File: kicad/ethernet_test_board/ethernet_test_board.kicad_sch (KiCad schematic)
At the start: 13 parts, among them J1 USB_C_Receptacle_USB2.0_16P, U1 W55RP20, U2 RT9080

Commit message: [add] kicad sch (finish) kicad pcb (WIP)
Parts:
- added C10, C11: 6.8n, Capacitor_SMD:C_0603_1608Metric, symbol Device:C
- added C12: 10n, Capacitor_SMD:C_0603_1608Metric, symbol Device:C
- added C13, C14: 18p, Capacitor_SMD:C_0603_1608Metric, symbol Device:C
- added C15, C16: 1μ, Capacitor_SMD:C_0603_1608Metric, symbol Device:C
- added C17, C18, C19, C20, C21: C, Capacitor_SMD:C_0603_1608Metric_Pad1.08x0.95mm_HandSolder, symbol Device:C
- added C5: 0.1μ, Capacitor_SMD:C_0603_1608Metric, symbol Device:C
- added C6: 0.1u, Capacitor_SMD:C_0603_1608Metric, symbol Device:C
- added C7: 10μ, Capacitor_SMD:C_0603_1608Metric, symbol Device:C
- added C8: 15p, Capacitor_SMD:C_0603_1608Metric, symbol Device:C
- added C9: 22n, Capacitor_SMD:C_0603_1608Metric, symbol Device:C
- added D1, D2: LED, Capacitor_SMD:C_0603_1608Metric, symbol Device:LED
- added D3: D, Capacitor_SMD:C_0603_1608Metric_Pad1.08x0.95mm_HandSolder, symbol Device:D
- added D4: LED, LED_SMD:LED_0603_1608Metric, symbol Device:LED
- added J2: Conn_01x02_Pin, ILG:ILG2pin, symbol Connector:Conn_01x02_Pin
- added J3, J5: TMJD4152NENLC, TMJD4152NENLC:TMJD4152NENLC, symbol TMJD4152NENLC:TMJD4152NENLC
- added J4: Conn_02x13_Top_Bottom, Connector_PinHeader_2.54mm:PinHeader_2x13_P2.54mm_Vertical, symbol Connector_Generic:Conn_02x13_Top_Bottom
- added J7: Micro_SD_Card_Det_Hirose_DM3AT, Connector_Card:microSD_HC_Hirose_DM3AT-SF-PEJM5, symbol Connector:Micro_SD_Card_Det_Hirose_DM3AT
- added J8: Conn_01x02_Pin, Connector_JST:JST_VH_B2P-VH-B_1x02_P3.96mm_Vertical, symbol Connector:Conn_01x02_Pin
- added R10, R11, R12, R13, R14, R9: 10K, Resistor_SMD:R_0603_1608Metric, symbol Device:R
- added R15: 100, Resistor_SMD:R_0603_1608Metric, symbol Device:R
- added R16, R17, R20, R21: 49.9, Capacitor_SMD:C_0603_1608Metric, symbol Device:R
- added R19: 10, Capacitor_SMD:C_0603_1608Metric, symbol Device:R
- added R22: 1M, Capacitor_SMD:C_0603_1608Metric, symbol Device:R
- added R23, R24: R, Capacitor_SMD:C_0603_1608Metric, symbol Device:R
- added R7: 10k, Resistor_SMD:R_0603_1608Metric, symbol Device:R
- added R8: 1k, Resistor_SMD:R_0603_1608Metric, symbol Device:R
- added SW1, SW2: SW_Push, Button_Switch_THT:SW_PUSH_6mm_H7.3mm, symbol Switch:SW_Push
- added U3: MCP25625-x-SS, Package_SO:SSOP-28_5.3x10.2mm_P0.65mm, symbol Interface_CAN_LIN:MCP25625-x-SS
- added U4: XC6201, Package_TO_SOT_SMD:SOT-23-5, symbol Regulator_Linear:XC6206PxxxMR
- added U5: SiT2001B, Package_TO_SOT_SMD:SOT-23-5, symbol Regulator_Linear:AP2127K-1.2
- added U6: LM66100DCKR, LM66100DCKR:SOT65P210X110-6N, symbol LM66100DCKR:LM66100DCKR
- added Y1: FA-128, Oscillator:Oscillator_SMD_SeikoEpson_SG210-4Pin_2.5x2.0mm, symbol Oscillator:SG-210SED
- C1, C2, C3, C4, R2, R3, R4, R5, R6: footprint (none) -> Capacitor_SMD:C_0603_1608Metric
- J1: footprint (none) -> Connector_USB:USB_C_Receptacle_GCT_USB4105-xx-A_16P_TopMnt_Horizontal
- R1: value 100k -> 1k; footprint (none) -> Capacitor_SMD:C_0603_1608Metric
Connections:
- net +3.3V: now also R2.1, C17.1, C18.1, C19.1, C20.1, C5.1, C6.1, C7.1, D4.2 (A), J3.11 (A_YELLOW), J3.13 (A_GREEN), J4.3 (Pin_3), J5.11 (A_YELLOW), J5.13 (A_GREEN), J7.4 (VDD), R10.2, R11.2, R12.2, R13.2, R14.2, R23.1, R24.2, R7.1, R9.2, U3.1 (VIO), U3.19 (VDD), U5.4 (NC); no longer U1.29 (RUN)
- net +5V: now also C16.1, C21.1, J4.4 (Pin_4), U3.27 (VDDA), U4.5 (VO), U6.6 (VOUT); no longer J1.A4 (VBUS), J1.A9 (VBUS), J1.B4 (VBUS), J1.B9 (VBUS)
- net GND: now also R3.2, C12.2, C13.2, C14.2, C15.2, C16.2, C17.2, C18.2, C19.2, C20.2, C21.2, C5.2, C6.2, C7.2, C8.2, C9.1, J3.10, J3.7, J4.26 (Pin_26), J5.10, J5.7, J7.11 (SHIELD), J7.6 (VSS), J7.9 (DET_B), J8.2 (Pin_2), R8.2, SW1.1, SW2.1, U3.10 (GND), U3.26 (VSS), U4.2 (GND), U5.1 (GND), U6.2 (GND), U6.3 (~{CE}), Y1.2 (GND), Y1.4 (GND)
- net USB_Minus: now also U1.57 (USB_DM); no longer R3.1
- net USB_Plus: now also U1.58 (UDB_DP); no longer R2.1
- net TXM: now reaches U1.1 (TXN)
- net TXM: now also J3.1 (TD-), J4.20 (Pin_20), J5.4 (RD-), R16.2
- net DAT3: now reaches U1.10 (GPIO5)
- net DAT3: now also J7.2 (DAT3/CD), R13.1
- net CLK: now reaches U1.11 (GPIO6)
- net CLK: now also J7.5 (CLK), R11.1
- net CMD: now reaches U1.12 (GPIO7)
- net CMD: now also J7.3 (CMD), R12.1
- net DAT1: now reaches U1.14 (GPIO8)
- net DAT1: now also J7.8 (DAT1), R9.1
- net DAT2: now reaches U1.15 (GPIO9)
- net DAT2: now also J7.1 (DAT2), R14.1
- net CAN_CLK: now reaches U1.16 (GPIO10)
- net CAN_CLK: now also U3.14 (SCK)
- net CAN_MOSI: now reaches U1.17 (GPIO11)
- net CAN_MOSI: now also U3.15 (SI)
- net CAN_MISO: now reaches U1.18 (GPIO12)
- net CAN_MISO: now also U3.16 (SO)
- net CAN_CS: now reaches U1.19 (GPIO13)
- net CAN_CS: now also U3.17 (~{CS})
- net TXP: now reaches U1.2 (TXP)
- net TXP: now also J3.3 (TD+), J4.21 (Pin_21), J5.6 (RD+), R17.2
- net CAN_STBY: now reaches U1.20 (GPIO14)
- net CAN_STBY: now also U3.5 (STBY)
- net GPIO15: now reaches U1.21 (GPIO15)
- net GPIO15: now also J4.18 (Pin_18)
- net CLK_OUT: now reaches U1.23 (XIN)
- net CLK_OUT: now also C8.1, U3.9 (OSC1), U5.5 (OUT)
- net SWCLK: now reaches U1.27 (SWCLK)
- net SWCLK: now also J4.24 (Pin_24)
- net SWD: now reaches U1.28 (SWD)
- net SWD: now also J4.25 (Pin_25)
- net GPIO16: now reaches U1.30 (GPIO16)
- net GPIO16: now also J4.19 (Pin_19)
- net SPEED: now reaches U1.36 (SPDLED)
- net SPEED: now also J3.12 (K_YELLOW), J5.12 (K_YELLOW)
- net LINK: now reaches U1.37 (LINKLED)
- net LINK: now also J3.14 (K_GREEN), J5.14 (K_GREEN)
- net DUPLEX: now reaches U1.38 (DUPLED)
- net DUPLEX: now also D2.1 (K)
- net ACTIVE: now reaches U1.39 (ACTLED)
- net ACTIVE: now also D1.1 (K)
- net RXM: now reaches U1.4 (RXN)
- net RXM: now also C10.1, J4.23 (Pin_23), R20.1
- net GPIO18: now reaches U1.40 (GPIO18)
- net GPIO18: now also J4.13 (Pin_13)
- net GPIO19: now reaches U1.41 (GPIO19)
- net GPIO19: now also J4.12 (Pin_12)
- net W5500_CLKIN: now reaches U1.44 (XI)
- net W5500_CLKIN: now also C14.1, R22.1, Y1.1 (OUT)
- net W5500_CLKOUT: now reaches U1.45 (XO)
- net W5500_CLKOUT: now also C13.1, R22.2, Y1.3 (OUT)
- net GPIO26: now reaches U1.46 (GPIO26/ADC0)
- net GPIO26: now also J4.11 (Pin_11)
- net GPIO27: now reaches U1.47 (GPIO27/ADC1)
- net GPIO27: now also J4.10 (Pin_10)
- net GPIO28: now reaches U1.48 (GPIO28/ADC2)
- net GPIO28: now also J4.9 (Pin_9)
- net GPIO29: now reaches U1.49 (GPIO29/ADC3)
- net GPIO29: now also J4.8 (Pin_8)
- net RXP: now reaches U1.5 (RXP)
- net RXP: now also C11.1, J4.22 (Pin_22), R21.1
- net PMODE2: now reaches U1.50 (PMODE2)
- net PMODE2: now also J4.5 (Pin_5)
- net PMODE1: now reaches U1.51 (PMODE1)
- net PMODE1: now also J4.6 (Pin_6)
- net PMODE0: now reaches U1.52 (PMODE0)
- net PMODE0: now also J4.7 (Pin_7)
- net at R2.2: now also U1.29 (RUN), SW1.2; no longer U1.58 (UDB_DP)
- net at R1.1, U1.63 (BOOT): now also SW2.2
- net GPIO0: now reaches U1.65 (GPIO0)
- net GPIO0: now also J4.14 (Pin_14)
- net GPIO1: now reaches U1.66 (GPIO1)
- net GPIO1: now also J4.15 (Pin_15)
- net GPIO2: now reaches U1.67 (GPIO2)
- net GPIO2: now also J4.16 (Pin_16)
- net GPIO3: now reaches U1.68 (GPIO3)
- net GPIO3: now also J4.17 (Pin_17)
- net DAT0: now reaches U1.9 (GPIO4)
- net DAT0: now also J7.7 (DAT0), R10.1
- new net: J7.10 (DET_A), R15.1
- new net: J2.1 (Pin_1), U3.3 (CANL)
- new net: J2.2 (Pin_2), U3.4 (CANH)
- new net: D1.2 (A), R23.2
- new net: D3.2 (A), J8.1 (Pin_1)
- new net: D4.1 (K), R15.2
- new net: C12.1, J3.5 (CT_2), J5.2 (CT_1), R20.2, R21.2
- new net: R7.2, U3.18 (~{RESET})
- new net: U3.20 (TxCAN), U3.28 (RXD)
- new net: U3.21 (RxCAN), U3.24 (TXD)
- new net: R8.1, U3.8 (OSC2)
- new net: C10.2, J3.4 (RD-), J5.1 (TD-)
- new net: C11.2, J3.6 (RD+), J5.3 (TD+)
- new net: C9.2, J3.2 (CT_1), J5.5 (CT_2), R19.2
- new net: R3.1, U6.5 (ST)
- new net: D2.2 (A), R24.1
- new net +3.3VA: R16.1, R17.1, R19.1
- new net +BATT: C15.1, D3.1 (K), J4.1 (Pin_1), U4.1 (VI)
- new net CAN_INT: U3.13 (~{INT})
- new net Ethernet_PoE: J3.9, J4.2 (Pin_2), J5.9
- new net USB_VCC: J1.A4 (VBUS), J1.A9 (VBUS), J1.B4 (VBUS), J1.B9 (VBUS), U6.1 (VIN)
- no-connect marks 3 -> 2
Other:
- note added: "GREEN_LINK"
- note added: "YELLOW_SPEED"
- note added: "microSD"
- moved on the sheet: C2, C3, R1, U2

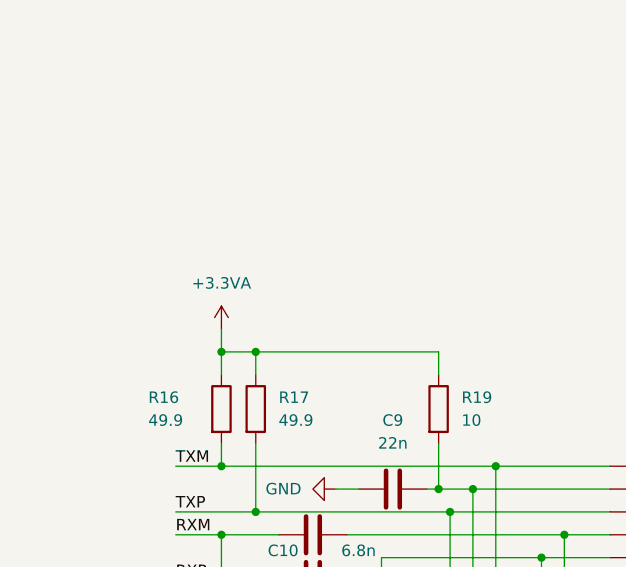
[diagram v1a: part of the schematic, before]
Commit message: [fix] kicad ethernet error
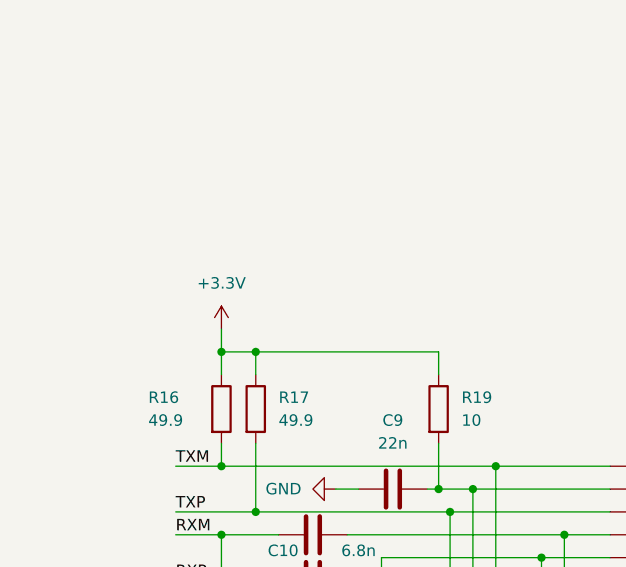
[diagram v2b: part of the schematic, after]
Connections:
- net +3.3VA is gone; now on net +3.3V: R16.1, R17.1, R19.1
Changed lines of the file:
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@@
 	)
 	(symbol
+		(lib_id "power:+3.3V")
+		(at -102.87 134.62 0)
+		(unit 1)
+		(exclude_from_sim no)
+		(in_bom yes)
+		(on_board yes)
+		(dnp no)
+		(fields_autoplaced yes)
+		(property "Reference" "#PWR034"
+			(at -102.87 138.43 0)
+			(effects
+				(font
+					(size 1.27 1.27)
+				)
+				(hide yes)
+			)
+		)
+		(property "Value" "+3.3V"
+			(at -102.87 129.54 0)
+			(effects
+				(font
+					(size 1.27 1.27)
+				)
+			)
+		)
+		(property "Footprint" ""
+			(at -102.87 134.62 0)
+			(effects
+				(font
+					(size 1.27 1.27)
+				)
+				(hide yes)
+			)
+		)
+		(property "Datasheet" ""
+			(at -102.87 134.62 0)
+			(effects
+				(font
+					(size 1.27 1.27)
+				)
+				(hide yes)
+			)
+		)
+		(property "Description" "Power symbol creates a global label with name \"+3.3V\""
+			(at -102.87 134.62 0)
+			(effects
+				(font
+					(size 1.27 1.27)
+				)
+				(hide yes)
+			)
+		)
+		(pin "1"
+		)
+		(instances
+			(project ""
+				(path "/72990fce-6b95-4e79-adfa-2df32c34bb5c"
+					(reference "#PWR034")
+					(unit 1)
+				)
+			)
+		)
+	)
+	(symbol
 		(lib_id "power:+5V")
 		(at 83.82 54.61 90)
@@
 					(unit 1)
 				)
-			)
-		)
-	)
-	(symbol
-		(lib_id "power:+3.3VA")
-		(at -102.87 134.62 0)
-		(unit 1)
-		(exclude_from_sim no)
-		(in_bom yes)
-		(on_board yes)
-		(dnp no)
-		(fields_autoplaced yes)
-		(property "Reference" "#PWR034"
-			(at -102.87 138.43 0)
-			(effects
-				(font
-					(size 1.27 1.27)
-				)
-				(hide yes)
-			)
-		)
-		(property "Value" "+3.3VA"
-			(at -102.87 129.54 0)
-			(effects
-				(font
-					(size 1.27 1.27)
-				)
-			)
-		)
-		(property "Footprint" ""
-			(at -102.87 134.62 0)
-			(effects
-				(font
-					(size 1.27 1.27)
-				)
-				(hide yes)
-			)
-		)
-		(property "Datasheet" ""
-			(at -102.87 134.62 0)
-			(effects
-				(font
-					(size 1.27 1.27)
-				)
-				(hide yes)
-			)
-		)
-		(property "Description" "Power symbol creates a global label with name \"+3.3VA\""
-			(at -102.87 134.62 0)
-			(effects
-				(font
-					(size 1.27 1.27)
-				)
-				(hide yes)
-			)
-		)
-		(pin "1"
-		)
-		(instances
-			(project ""
-				(path "/72990fce-6b95-4e79-adfa-2df32c34bb5c"
-					(reference "#PWR034")
-					(unit 1)
-				)

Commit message: [add] kicad pcb
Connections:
- net +5V: now also U6.3 (~{CE})
- net GND: no longer U6.3 (~{CE})
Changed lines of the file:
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@@
 	(wire
 		(pts
-			(xy 35.56 168.91) (xy 35.56 166.37)
-		)
-		(stroke
-			(width 0)
-			(type default)
-		)
-	)
-	(wire
-		(pts
 			(xy 323.85 69.85) (xy 314.96 69.85)
 		)
@@
 	)
 	(symbol
-		(lib_id "Connector_Generic:Conn_02x13_Top_Bottom")
-		(at 328.93 67.31 0)
-		(unit 1)
-		(exclude_from_sim no)
-		(in_bom yes)
-		(on_board yes)
-		(dnp no)
-		(fields_autoplaced yes)
-		(property "Reference" "J4"
-			(at 330.2 45.72 0)
-			(effects
-				(font
-					(size 1.27 1.27)
-				)
-			)
-		)
-		(property "Value" "Conn_02x13_Top_Bottom"
-			(at 330.2 48.26 0)
-			(effects
-				(font
-					(size 1.27 1.27)
-				)
-			)
-		)
-		(property "Footprint" "Connector_PinHeader_2.54mm:PinHeader_2x13_P2.54mm_Vertical"
-			(at 328.93 67.31 0)
-			(effects
-				(font
-					(size 1.27 1.27)
-				)
-				(hide yes)
-			)
-		)
-		(property "Datasheet" "~"
-			(at 328.93 67.31 0)
-			(effects
-				(font
-					(size 1.27 1.27)
-				)
-				(hide yes)
-			)
-		)
-		(property "Description" "Generic connector, double row, 02x13, top/bottom pin numbering scheme (row 1: 1...pins_per_row, row2: pins_per_row+1 ... num_pins), script generated (kicad-library-utils/schlib/autogen/connector/)"
-			(at 328.93 67.31 0)
-			(effects
-				(font
-					(size 1.27 1.27)
-				)
-				(hide yes)
-			)
-		)
-		(pin "26"
-		)
-		(pin "17"
-		)
-		(pin "19"
-		)
-		(pin "11"
-		)
-		(pin "12"
-		)
-		(pin "13"
-		)
-		(pin "4"
-		)
-		(pin "15"
-		)
-		(pin "14"
-		)
-		(pin "21"
-		)
-		(pin "2"
-		)
-		(pin "10"
-		)
-		(pin "1"
-		)
-		(pin "6"
-		)
-		(pin "5"
-		)
-		(pin "9"
-		)
-		(pin "16"
-		)
-		(pin "20"
-		)
-		(pin "25"
-		)
-		(pin "3"
-		)
-		(pin "22"
-		)
-		(pin "23"
-		)
-		(pin "8"
-		)
-		(pin "7"
-		)
-		(pin "18"
-		)
-		(pin "24"
-		)
-		(instances
-			(project ""
-				(path "/72990fce-6b95-4e79-adfa-2df32c34bb5c"
-					(reference "J4")
-					(unit 1)
-				)
-			)
-		)
-	)
-	(symbol
 		(lib_id "power:+3.3V")
 		(at 256.54 24.13 0)
@@
 	)
 	(symbol
+		(lib_id "Connector_Generic:Conn_02x13_Top_Bottom")
+		(at 328.93 67.31 0)
+		(unit 1)
+		(exclude_from_sim no)
+		(in_bom yes)
+		(on_board yes)
+		(dnp no)
+		(fields_autoplaced yes)
+		(property "Reference" "J4"
+			(at 330.2 45.72 0)
+			(effects
+				(font
+					(size 1.27 1.27)
+				)
+			)
+		)
+		(property "Value" "Conn_02x13_Top_Bottom"
+			(at 330.2 48.26 0)
+			(effects
+				(font
+					(size 1.27 1.27)
+				)
+			)
+		)
+		(property "Footprint" "Connector_PinHeader_2.54mm:PinHeader_2x13_P2.54mm_Vertical"
+			(at 328.93 67.31 0)
+			(effects
+				(font
+					(size 1.27 1.27)
+				)
+				(hide yes)
+			)
+		)
+		(property "Datasheet" "~"
+			(at 328.93 67.31 0)
+			(effects
+				(font
+					(size 1.27 1.27)
+				)
+				(hide yes)
+			)
+		)
+		(property "Description" "Generic connector, double row, 02x13, top/bottom pin numbering scheme (row 1: 1...pins_per_row, row2: pins_per_row+1 ... num_pins), script generated (kicad-library-utils/schlib/autogen/connector/)"
+			(at 328.93 67.31 0)
+			(effects
+				(font
+					(size 1.27 1.27)
+				)
+				(hide yes)
+			)
+		)
+		(pin "17"
+		)
+		(pin "16"
+		)
+		(pin "26"
+		)
+		(pin "21"
+		)
+		(pin "19"
+		)
+		(pin "18"
+		)
+		(pin "10"
+		)
+		(pin "7"
+		)
+		(pin "6"
+		)
+		(pin "5"
+		)
+		(pin "4"
+		)
+		(pin "3"
+		)
+		(pin "2"
+		)
+		(pin "1"
+		)
+		(pin "15"
+		)
+		(pin "14"
+		)
+		(pin "13"
+		)
+		(pin "22"
+		)
+		(pin "23"
+		)
+		(pin "25"
+		)
+		(pin "24"
+		)
+		(pin "11"
+		)
+		(pin "12"
+		)
+		(pin "9"
+		)
+		(pin "20"
+		)
+		(pin "8"
+		)
+		(instances
+			(project ""
+				(path "/72990fce-6b95-4e79-adfa-2df32c34bb5c"
+					(reference "J4")
+					(unit 1)
+				)
+			)
+		)
+	)
+	(symbol
 		(lib_id "power:+BATT")
 		(at 80.01 25.4 90)
@@
 	)
 	(symbol
-		(lib_id "power:GND")
-		(at 35.56 168.91 0)
-		(unit 1)
-		(exclude_from_sim no)
-		(in_bom yes)
-		(on_board yes)
-		(dnp no)
-		(fields_autoplaced yes)
-		(property "Reference" "#PWR052"
-			(at 35.56 175.26 0)
-			(effects
-				(font
-					(size 1.27 1.27)
-				)
-				(hide yes)
-			)
-		)
-		(property "Value" "GND"
-			(at 35.56 173.99 0)
-			(effects
-				(font
-					(size 1.27 1.27)
-				)
-			)
-		)
-		(property "Footprint" ""
-			(at 35.56 168.91 0)
-			(effects
-				(font
-					(size 1.27 1.27)
-				)
-				(hide yes)
-			)
-		)
-		(property "Datasheet" ""
-			(at 35.56 168.91 0)
-			(effects
-				(font
-					(size 1.27 1.27)
-				)
-				(hide yes)
-			)
-		)
-		(property "Description" "Power symbol creates a global label with name \"GND\" , ground"
-			(at 35.56 168.91 0)
-			(effects
-				(font
-					(size 1.27 1.27)
-				)
-				(hide yes)
-			)
-		)
-		(pin "1"
-		)
-		(instances
-			(project "ethernet_test_board"
-				(path "/72990fce-6b95-4e79-adfa-2df32c34bb5c"
-					(reference "#PWR052")
-					(unit 1)
-				)
-			)
-		)
-	)
-	(symbol
 		(lib_id "Device:C")
 		(at 358.14 27.94 0)
@@
 					(unit 1)
 				)
+			)
+		)
+	)
+	(symbol
+		(lib_id "power:+5V")
+		(at 35.56 166.37 90)
+		(unit 1)
+		(exclude_from_sim no)
+		(in_bom yes)
+		(on_board yes)
+		(dnp no)
+		(fields_autoplaced yes)
+		(property "Reference" "#PWR052"
+			(at 39.37 166.37 0)
+			(effects
+				(font
+					(size 1.27 1.27)
+				)
+				(hide yes)
+			)
+		)
+		(property "Value" "+5V"
+			(at 31.75 166.3699 90)
+			(effects
+				(font
+					(size 1.27 1.27)
+				)
+				(justify left)
+			)
+		)
+		(property "Footprint" ""
+			(at 35.56 166.37 0)
+			(effects
+				(font
+					(size 1.27 1.27)
+				)
+				(hide yes)
+			)
+		)
+		(property "Datasheet" ""
+			(at 35.56 166.37 0)
+			(effects
+				(font
+					(size 1.27 1.27)
+				)
+				(hide yes)
+			)
+		)
+		(property "Description" "Power symbol creates a global label with name \"+5V\""
+			(at 35.56 166.37 0)
+			(effects
+				(font
+					(size 1.27 1.27)
+				)
+				(hide yes)
+			)
+		)
+		(pin "1"
+		)
+		(instances
+			(project ""
+				(path "/72990fce-6b95-4e79-adfa-2df32c34bb5c"
+					(reference "#PWR052")
+					(unit 1)
+				)
